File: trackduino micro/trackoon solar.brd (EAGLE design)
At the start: 19.1 x 59.3 mm, 62 parts, among them IC1 MCP73871, IC2 74AHC1G125DBV, SW1 SPST_TACT-KMR2, U1 ATMEGA168MLF, Y1 16MHZ

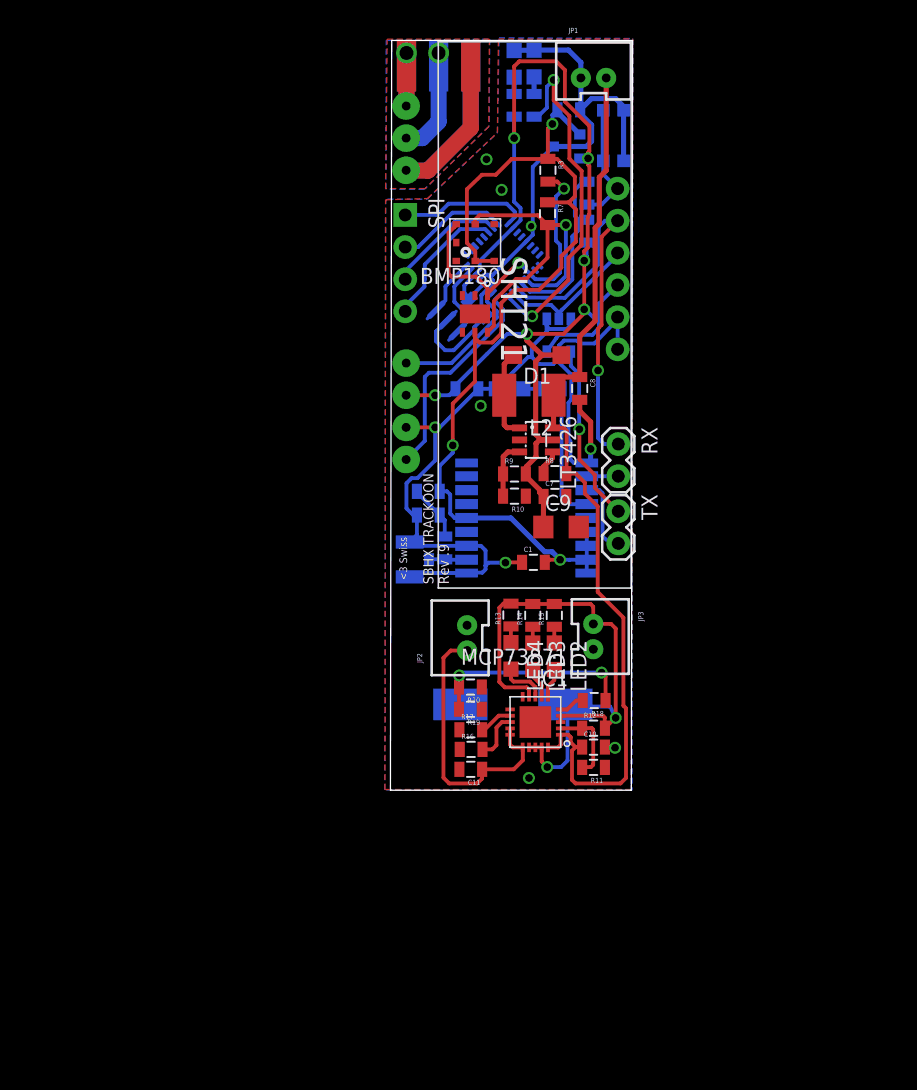
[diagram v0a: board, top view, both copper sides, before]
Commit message: solar board routing
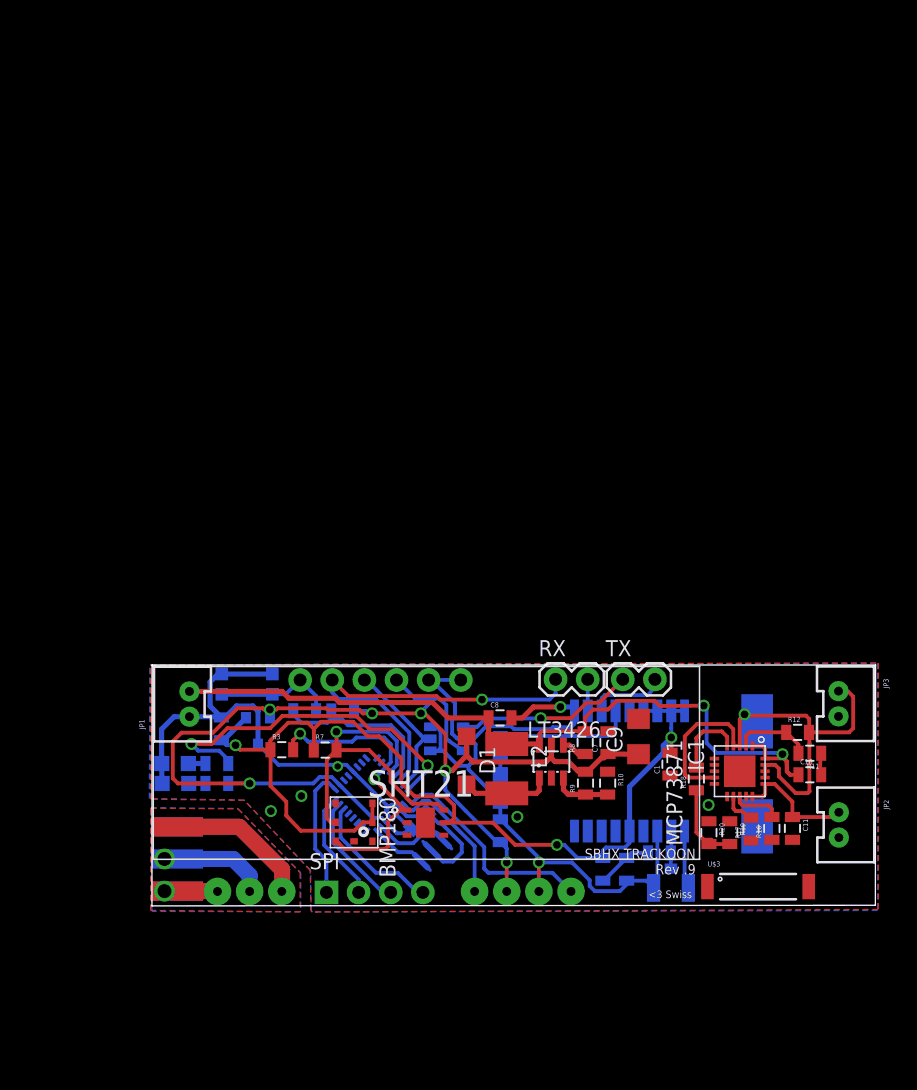
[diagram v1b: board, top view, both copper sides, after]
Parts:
- removed LED2, LED3, LED4: (no value), adafruit:CHIPLED_0805
- removed R13, R14, R15: 1k, SparkFun-Resistors:0805
- added U$3: ANTENNA2SMD3, SparkFun-RF:ANTENNA-CHIP4
- moved J$1 67.7 mm to (10.8, 13.0), turned to 90 degrees
- moved VCC 62.9 mm to (10.7, 21.5), turned to 270 degrees
- moved FRAME1 62.3 mm to (23.2, 3.68), turned to 0 degrees
- moved PTT 62.2 mm to (10.6, 23.1), turned to 270 degrees
- moved JP1 59.7 mm to (11.2, 27.8), turned to 90 degrees
- moved R4 58.5 mm to (13.9, 21.5), turned to 180 degrees
- moved R6 57.7 mm to (13.9, 23.1), turned to 180 degrees
- moved C2 56.1 mm to (14.3, 25.8), turned to 270 degrees
- moved SPI 53.9 mm to (22.6, 12.9), turned to 0 degrees
- moved LM3480 52.2 mm to (17.2, 25.7), turned to 180 degrees
- moved SW1 52.1 mm to (16.3, 29.4), turned to 180 degrees
- moved R3 50.4 mm to (19.1, 24.2), turned to 0 degrees
- moved BMP180 46.8 mm to (24.8, 18.4), turned to 270 degrees
- moved C5 46.6 mm to (20.9, 27.3), turned to 0 degrees
- moved FTDI 46.2 mm to (20.5, 29.7), turned to 180 degrees
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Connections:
- removed net N$19: LED2.A, R15.1
- removed net N$20: LED3.A, R14.1
- removed net N$21: LED4.A, R13.1
- removed net N$22: IC1.6, LED2.C
- removed net STAT1: IC1.8, LED4.C
- removed net STAT2: IC1.7, LED3.C
- net VSOLAR: no longer R13.2, R14.2, R15.2
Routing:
- net VBATT: track 22.6 -> 10.4 mm
- net 15V: track 72.8 -> 62.8 mm, vias 0 -> 2
- net N$30: track 16.4 -> 6.78 mm, vias 2 -> 0
- net VSOLAR: track 46.8 -> 39.9 mm, vias 2 -> 1
- net GND: track 151.3 -> 144.6 mm, vias 10 -> 8
- net N$29: track 2.05 -> 5.89 mm
- net STAT1: track 3.74 -> 0.00 mm
- net STAT2: track 2.45 -> 0.00 mm
- net N$22: track 2.36 -> 0.00 mm
- net N$21: track 1.28 -> 0.00 mm
- net N$20: track 1.28 -> 0.00 mm
- net N$19: track 1.28 -> 0.00 mm
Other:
- board size 19.1 x 59.3 mm -> 57.2 x 19 mm

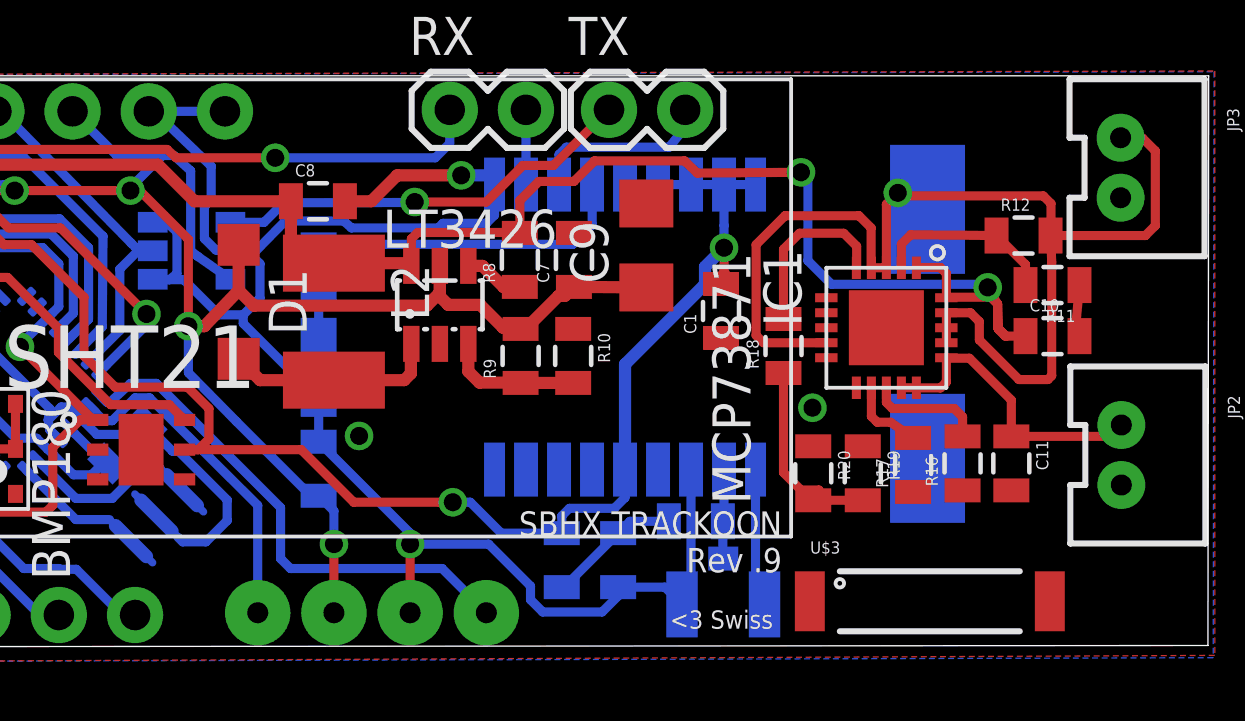
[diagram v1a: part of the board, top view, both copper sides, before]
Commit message: solar replace antenna
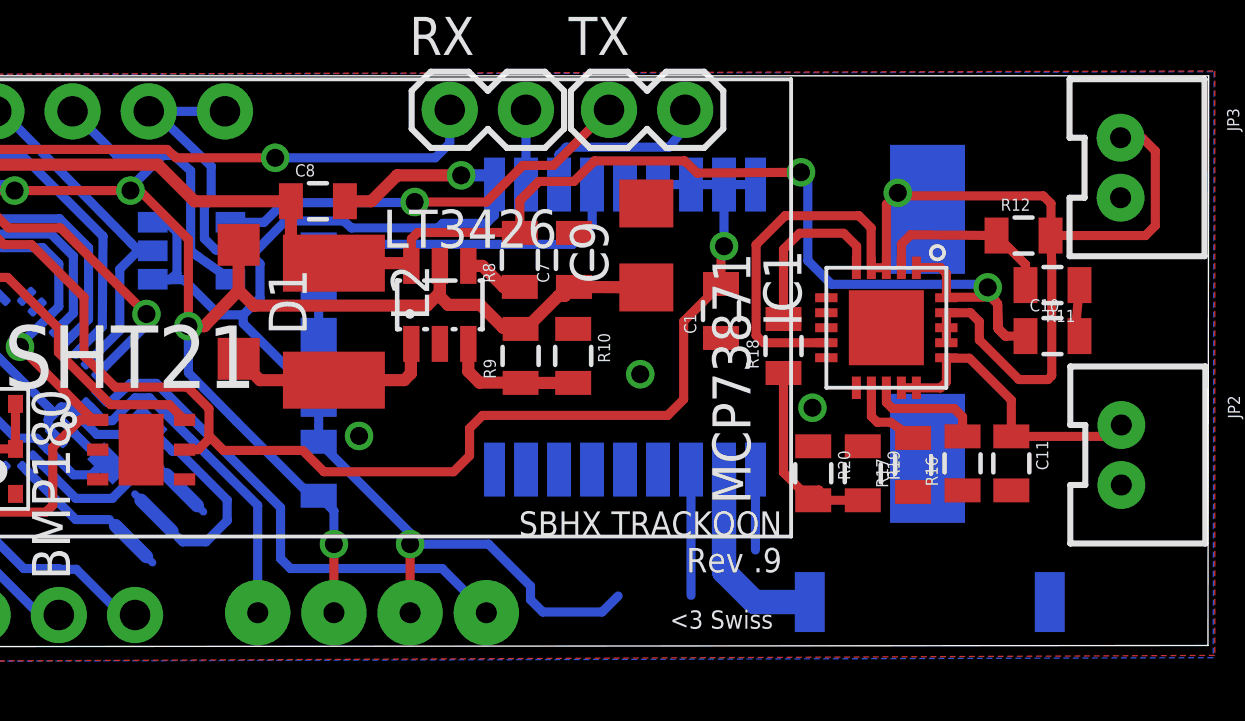
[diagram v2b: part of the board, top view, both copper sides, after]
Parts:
- removed C6: 47pf, SparkFun-Capacitors:0805
- removed L1: 27nh, SparkFun-Passives:0805
- removed R2: 10ohm, SparkFun-Resistors:0805
- removed X1: (no value), adafruit:U.FL
- flipped U$3 to the bottom, turned to 180 degrees
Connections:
- removed net N$24: C6.1, L1.2, R2.1
- net 3V: no longer R2.2, U$1.14_VCC_RF
- net GND: no longer C6.2, X1.1, X1.2
- net N$6: now also U$3.SIG; no longer L1.1, X1.3
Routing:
- net GND: track 144.6 -> 139.5 mm, vias 8 -> 9
- net 3V: track 79.0 -> 74.4 mm, vias 3 -> 2
- net N$24: track 4.48 -> 0.00 mm
- net N$6: track 2.98 -> 6.68 mm

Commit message: solar ground plane fix
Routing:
- net GND: track 139.5 -> 124.3 mm
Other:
- board size 57.2 x 19 mm -> 57.2 x 19.1 mm
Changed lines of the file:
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@@
 <board>
 <plain>
-<wire x1="8.8138" y1="11.8364" x2="65.9894" y2="11.8872" width="0" layer="20"/>
-<wire x1="65.9894" y1="11.8872" x2="66.0148" y2="30.8764" width="0" layer="20"/>
+<wire x1="8.8138" y1="11.8364" x2="66.0148" y2="11.811" width="0" layer="20"/>
+<wire x1="66.0148" y1="11.811" x2="66.0148" y2="30.8764" width="0" layer="20"/>
 <wire x1="66.0148" y1="30.8764" x2="8.8138" y2="30.8764" width="0" layer="20"/>
 <wire x1="8.8138" y1="30.8764" x2="8.8138" y2="11.8364" width="0" layer="20"/>
@@
 <vertex x="8.6868" y="30.8864"/>
 <vertex x="66.2178" y="31.0388"/>
-<vertex x="66.2178" y="11.557"/>
+<vertex x="66.2432" y="16.2306"/>
+<vertex x="50.3936" y="16.2306"/>
+<vertex x="50.3936" y="11.5062"/>
 <vertex x="21.4122" y="11.3538"/>
 <vertex x="21.3106" y="14.6558"/>
@@
 <vertex x="8.6614" y="30.8864"/>
 <vertex x="66.1924" y="31.0134"/>
-<vertex x="66.167" y="11.4808"/>
+<vertex x="66.2432" y="16.1798"/>
+<vertex x="50.3936" y="16.1798"/>
+<vertex x="50.3936" y="11.4808"/>
 <vertex x="21.5138" y="11.3538"/>
 <vertex x="21.3614" y="11.5062"/>
@@
 <wire x1="24.702478125" y1="22.463275" x2="27.3812" y2="19.784553125" width="0.3048" layer="16"/>
 <wire x1="27.3812" y1="19.784553125" x2="27.3304" y2="19.4056" width="0.3048" layer="16"/>
-<wire x1="48.759" y1="17.7512" x2="48.759" y2="13.558" width="0.3048" layer="16"/>
-<wire x1="50.909" y1="17.7512" x2="50.9056" y2="15.0696" width="0.3048" layer="16"/>
 <wire x1="36.3474" y1="20.1082" x2="36.3474" y2="18.68" width="0.3048" layer="16"/>
 <wire x1="17.1958" y1="24.6048" x2="18.8136" y2="22.987" width="0.3048" layer="16"/>
@@
 <wire x1="39.3954" y1="15.2654" x2="39.3954" y2="15.632" width="0.3048" layer="16"/>
 <wire x1="39.3954" y1="15.632" x2="36.3474" y2="18.68" width="0.3048" layer="16"/>
-<wire x1="46.3296" y1="13.5382" x2="45.7962" y2="13.0048" width="0.3048" layer="16"/>
-<wire x1="45.7962" y1="13.0048" x2="43.815" y2="13.0048" width="0.3048" layer="16"/>
-<wire x1="43.815" y1="13.0048" x2="43.4086" y2="13.4112" width="0.3048" layer="16"/>
-<wire x1="43.4086" y1="13.4112" x2="43.4086" y2="13.8684" width="0.3048" layer="16"/>
-<wire x1="43.4086" y1="13.8684" x2="42.0116" y2="15.2654" width="0.3048" layer="16"/>
-<wire x1="42.0116" y1="15.2654" x2="39.3954" y2="15.2654" width="0.3048" layer="16"/>
 <wire x1="10.8204" y1="18.0848" x2="15.7226" y2="18.0848" width="1.27" layer="1"/>
 <wire x1="15.7226" y1="18.0848" x2="19.1008" y2="14.7066" width="1.27" layer="1"/>
@@
 <wire x1="55.2704" y1="24.479" x2="55.2704" y2="26.5938" width="0.3048" layer="1"/>
 <wire x1="55.2704" y1="26.5938" x2="55.5498" y2="26.8732" width="0.3048" layer="1"/>
-<via x="55.6514" y="26.9748" extent="1-16" drill="0.6" shape="square"/>
-<wire x1="55.5498" y1="26.8732" x2="55.6514" y2="26.9748" width="0.3048" layer="1"/>
-<wire x1="55.6514" y1="26.9748" x2="56.093" y2="26.9748" width="0.3048" layer="16"/>
-<wire x1="56.093" y1="26.9748" x2="56.642" y2="26.4258" width="0.3048" layer="16"/>
+<via x="55.88" y="26.8732" extent="1-16" drill="0.6" shape="square"/>
+<wire x1="55.5498" y1="26.8732" x2="55.88" y2="26.8732" width="0.3048" layer="1"/>
+<wire x1="55.88" y1="26.8732" x2="56.3216" y2="26.8732" width="0.3048" layer="16"/>
+<wire x1="56.3216" y1="26.8732" x2="56.642" y2="26.4258" width="0.3048" layer="16"/>
 <wire x1="60.7424" y1="25.5524" x2="63.9064" y2="25.5524" width="0.3048" layer="1"/>
 <wire x1="63.9064" y1="25.5524" x2="64.2366" y2="25.8826" width="0.3048" layer="1"/>
@@
 <wire x1="63.8048" y1="28.8036" x2="63.0864" y2="28.8036" width="0.3048" layer="1"/>
 <wire x1="63.0864" y1="28.8036" x2="63.077" y2="28.813" width="0.3048" layer="1"/>
-<wire x1="55.5498" y1="26.8732" x2="60.5028" y2="26.8732" width="0.3048" layer="1"/>
+<wire x1="55.88" y1="26.8732" x2="60.5028" y2="26.8732" width="0.3048" layer="1"/>
 <wire x1="60.5028" y1="26.8732" x2="60.7568" y2="26.6192" width="0.3048" layer="1"/>
 <wire x1="60.7568" y1="26.6192" x2="60.7568" y2="25.5668" width="0.3048" layer="1"/>

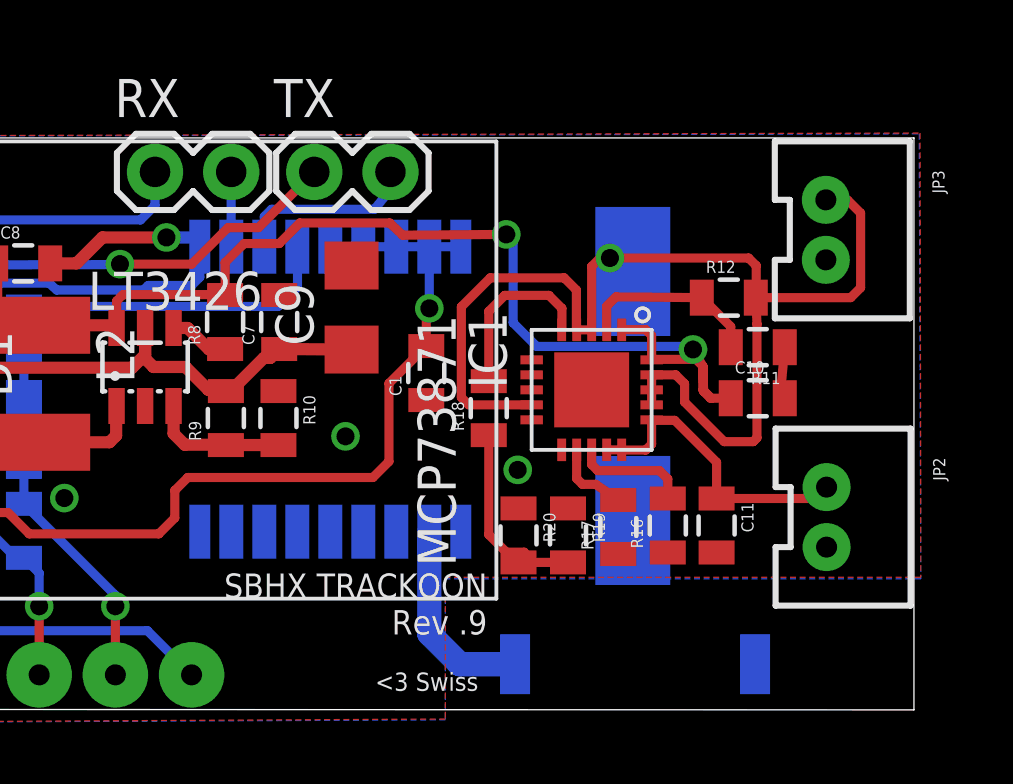
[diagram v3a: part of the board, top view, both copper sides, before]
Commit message: fixed overlaps on solar
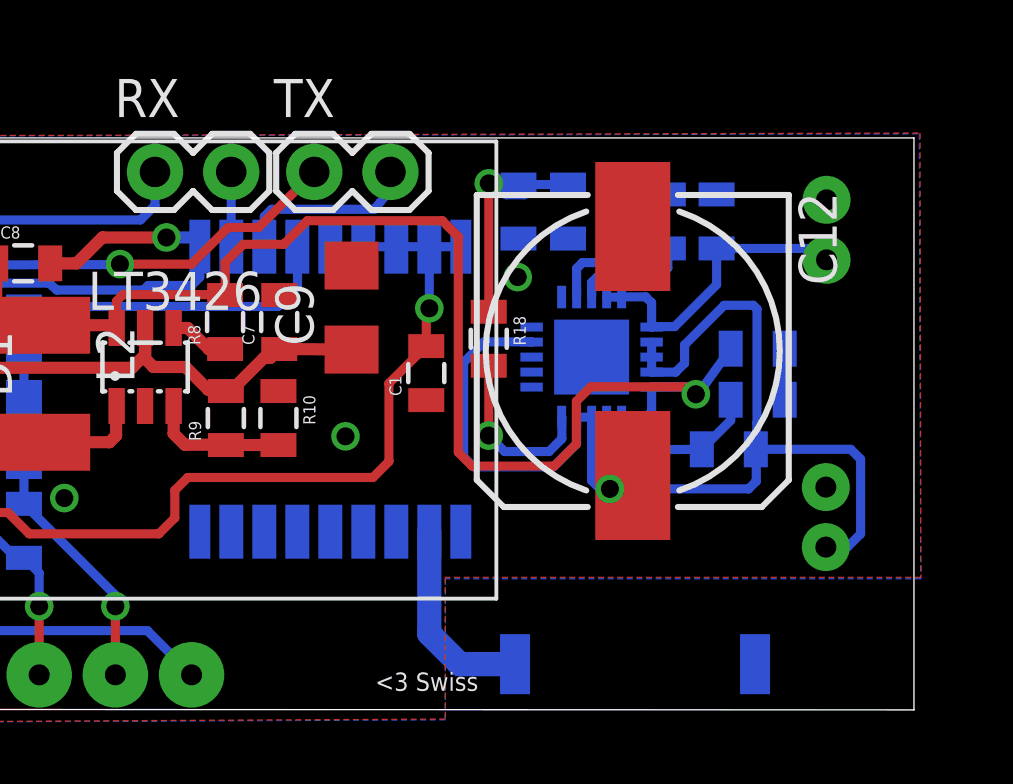
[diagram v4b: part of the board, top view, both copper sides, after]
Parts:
- moved R19 10.8 mm to (54.5, 28.4), flipped to the bottom, turned to 90 degrees
- moved R20 10.8 mm to (52.8, 28.4), flipped to the bottom, turned to 90 degrees
- moved R17 10.2 mm to (56.2, 28.1), flipped to the bottom, turned to 270 degrees
- moved C11 10.1 mm to (59.4, 28.1), flipped to the bottom, turned to 90 degrees
- moved R16 10.1 mm to (57.8, 28.1), flipped to the bottom, turned to 270 degrees
- moved JP2 9.58 mm to (63.7, 27.8), flipped to the bottom, turned to 90 degrees
- moved JP3 9.58 mm to (63.6, 18.2), flipped to the bottom, turned to 90 degrees
- moved R12 5.05 mm to (59.8, 20.5), flipped to the bottom, turned to 180 degrees
- moved R18 2.31 mm to (51.8, 24.2), turned to 270 degrees
- moved R11 1.75 mm to (60.8, 22.1), flipped to the bottom, turned to 0 degrees
- moved C10 1.65 mm to (60.8, 23.9), flipped to the bottom, turned to 180 degrees
- moved C12 1.50 mm to (56.6, 23.8), flipped to the top, turned to 270 degrees
- moved IC1 1.09 mm to (55.3, 23.6), flipped to the bottom, turned to 90 degrees
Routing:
- net 15V: track 62.8 -> 67.3 mm, vias 2 -> 1
- net N$30: track 6.78 -> 7.62 mm, vias 0 -> 1
- net N$29: vias 0 -> 1

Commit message: stuff
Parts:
- moved C10 0.15 mm to (61.0, 23.9)
- moved R11 0.15 mm to (61.0, 22.1)
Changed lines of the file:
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@@
 </element>
 <element name="IC1" library="adafruit" package="QFN20" value="MCP73871" x="55.2704" y="23.5712" rot="MR90"/>
-<element name="R11" library="SparkFun-Resistors" package="0805" value="100k" x="60.8076" y="22.1488" rot="MR0"/>
+<element name="R11" library="SparkFun-Resistors" package="0805" value="100k" x="60.96" y="22.1488" rot="MR0"/>
 <element name="R12" library="SparkFun-Resistors" package="0805" value="270k" x="59.8424" y="20.4978" rot="MR180"/>
 <element name="R16" library="SparkFun-Resistors" package="0805" value="2k" x="57.8104" y="28.0924" rot="MR270"/>
 <element name="R17" library="SparkFun-Resistors" package="0805" value="100k" x="56.1594" y="28.1432" rot="MR270"/>
-<element name="C10" library="SparkFun-Capacitors" package="0805" value="10uf" x="60.8076" y="23.8506" rot="MR180"/>
+<element name="C10" library="SparkFun-Capacitors" package="0805" value="10uf" x="60.96" y="23.8506" rot="MR180"/>
 <element name="JP2" library="SparkFun-Connectors" package="JST-2-PTH-VERT" value="M02JST-PTH-VERT" x="63.6524" y="27.813" rot="MR90"/>
 <element name="C11" library="SparkFun-Capacitors" package="0805" value="10uf" x="59.436" y="28.0924" rot="MR90"/>
@@
 <contactref element="JP3" pad="2"/>
 <contactref element="C12" pad="-"/>
-<wire x1="61.7076" y1="22.1488" x2="61.5552" y2="23.8252" width="0.3048" layer="16"/>
-<wire x1="61.5552" y1="23.8252" x2="61.7076" y2="23.8506" width="0.3048" layer="16"/>
+<wire x1="61.86" y1="22.1488" x2="61.5552" y2="23.8252" width="0.3048" layer="16"/>
+<wire x1="61.5552" y1="23.8252" x2="61.86" y2="23.8506" width="0.3048" layer="16"/>
 <via x="52.8066" y="26.2382" extent="1-16" drill="0.6"/>
 <via x="47.0662" y="20.9296" extent="1-16" drill="0.6"/>
@@
 <wire x1="57.2704" y1="22.5712" x2="58.6282" y2="22.5712" width="0.3048" layer="16"/>
 <wire x1="58.6282" y1="22.5712" x2="58.7447" y2="22.3321" width="0.3048" layer="16"/>
-<wire x1="58.9987" y1="22.5861" x2="59.9076" y2="23.8506" width="0.3048" layer="16"/>
+<wire x1="58.9987" y1="22.5861" x2="60.06" y2="23.8506" width="0.3048" layer="16"/>
 <wire x1="43.053" y1="25.6396" x2="43.053" y2="26.7208" width="0.3048" layer="1"/>
 <wire x1="43.053" y1="26.7208" x2="43.6626" y2="27.3304" width="0.3048" layer="1"/>
@@
 <wire x1="55.7704" y1="20.7852" x2="56.0832" y2="20.4724" width="0.3048" layer="16"/>
 <wire x1="56.0832" y1="20.4724" x2="58.9424" y2="20.4978" width="0.3048" layer="16"/>
-<wire x1="59.9076" y1="22.1488" x2="59.9076" y2="21.463" width="0.3048" layer="16"/>
+<wire x1="60.06" y1="22.1488" x2="59.9076" y2="21.463" width="0.3048" layer="16"/>
 <wire x1="59.9076" y1="21.463" x2="58.9424" y2="20.4978" width="0.3048" layer="16"/>
 </signal>
